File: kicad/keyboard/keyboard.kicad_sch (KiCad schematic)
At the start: 119 parts, among them SW1 MX_SWITCH, SW10 MX_SWITCH, SW11 MX_SWITCH, SW12 MX_SWITCH, SW13 MX_SWITCH, SW14 MX_SWITCH, SW15 MX_SWITCH, SW16 MX_SWITCH, SW17 MX_SWITCH, SW18 MX_SWITCH, SW19 MX_SWITCH, SW2 MX_SWITCH, SW20 MX_SWITCH, SW21 MX_SWITCH, SW22 MX_SWITCH, SW23 MX_SWITCH, SW24 MX_SWITCH, SW25 MX_SWITCH, SW26 MX_SWITCH, SW27 MX_SWITCH, SW28 MX_SWITCH, SW29 MX_SWITCH, SW3 MX_SWITCH, SW30 MX_SWITCH, SW31 MX_SWITCH, SW32 MX_SWITCH, SW33 MX_SWITCH, SW34 MX_SWITCH, SW35 MX_SWITCH, SW36 MX_SWITCH, SW37 MX_SWITCH, SW38 MX_SWITCH, SW39 MX_SWITCH, SW4 MX_SWITCH, SW40 MX_SWITCH, SW41 MX_SWITCH, SW42 MX_SWITCH, SW43 MX_SWITCH, SW44 MX_SWITCH, SW45 MX_SWITCH, SW46 MX_SWITCH, SW47 MX_SWITCH, SW48 MX_SWITCH, SW49 MX_SWITCH, SW5 MX_SWITCH, SW50 MX_SWITCH, SW51 MX_SWITCH, SW52 MX_SWITCH, SW53 MX_SWITCH, SW54 MX_SWITCH, SW55 MX_SWITCH, SW56 MX_SWITCH, SW57 MX_SWITCH, SW58 MX_SWITCH, SW59 MX_SWITCH, SW6 MX_SWITCH, SW7 MX_SWITCH, SW8 MX_SWITCH, SW9 MX_SWITCH

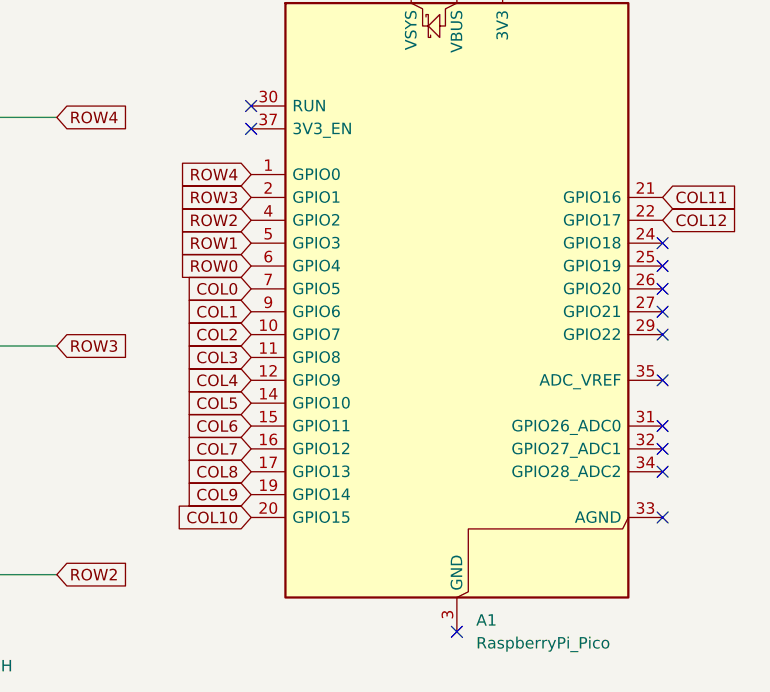
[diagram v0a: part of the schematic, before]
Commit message: Assign footprints
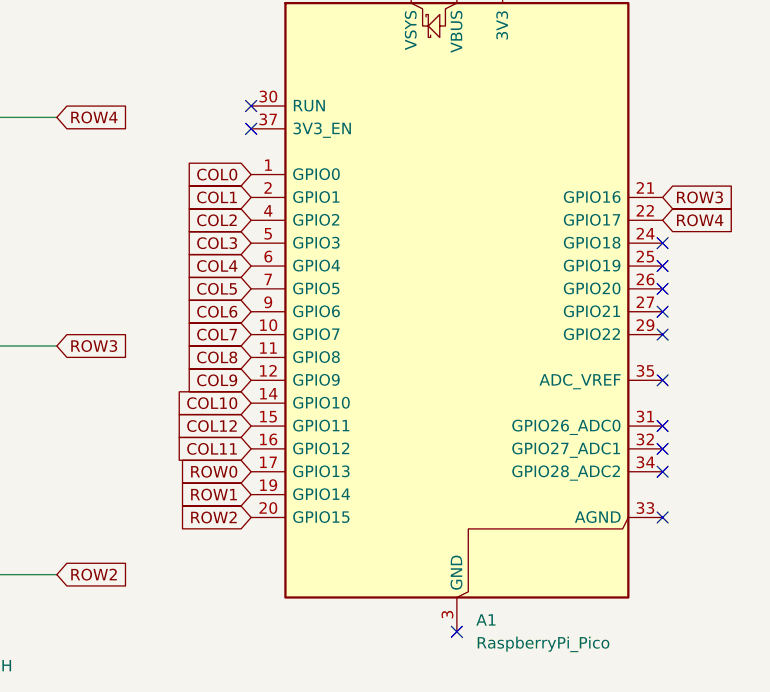
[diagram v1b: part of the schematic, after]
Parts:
- A1: footprint Module:RaspberryPi_Pico_Common_Unspecified -> Module:RaspberryPi_Pico_Common_THT
- D1, D10, D11, D12, D13, D14, D15, D16, D17, D18, D19, D2, D20, D21, D22, D23, D24, D25, D26, D27, D28, D29, D3, D30, D31, D32, D33, D34, D35, D36, D37, D38, D39, D4, D40, D41, D42, D43, D44, D45, D46, D47, D48, D49, D5, D50, D51, D52, D53, D54, D55, D56, D57, D58, D59, D6, D7, D8, D9: footprint (none) -> Diode_THT:D_DO-35_SOD27_P2.54mm_Vertical_KathodeUp
- SW1, SW10, SW11, SW12, SW13, SW14, SW15, SW16, SW17, SW18, SW19, SW2, SW20, SW21, SW22, SW23, SW24, SW25, SW26, SW27, SW28, SW29, SW3, SW30, SW31, SW32, SW33, SW34, SW35, SW36, SW37, SW38, SW39, SW4, SW40, SW41, SW42, SW43, SW44, SW45, SW46, SW47, SW48, SW49, SW5, SW50, SW51, SW52, SW53, SW54, SW55, SW56, SW57, SW58, SW59, SW6, SW7, SW8, SW9: footprint (none) -> Button_Switch_Keyboard:SW_Cherry_MX_1.00u_PCB
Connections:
- net COL0: now also A1.1 (GPIO0); no longer A1.7 (GPIO5)
- net COL1: now also A1.2 (GPIO1); no longer A1.9 (GPIO6)
- net COL10: now also A1.14 (GPIO10); no longer A1.20 (GPIO15)
- net COL11: now also A1.16 (GPIO12); no longer A1.21 (GPIO16)
- net COL12: now also A1.15 (GPIO11); no longer A1.22 (GPIO17)
- net COL2: now also A1.4 (GPIO2); no longer A1.10 (GPIO7)
- net COL3: now also A1.5 (GPIO3); no longer A1.11 (GPIO8)
- net COL4: now also A1.6 (GPIO4); no longer A1.12 (GPIO9)
- net COL5: now also A1.7 (GPIO5); no longer A1.14 (GPIO10)
- net COL6: now also A1.9 (GPIO6); no longer A1.15 (GPIO11)
- net COL7: now also A1.10 (GPIO7); no longer A1.16 (GPIO12)
- net COL8: now also A1.11 (GPIO8); no longer A1.17 (GPIO13)
- net COL9: now also A1.12 (GPIO9); no longer A1.19 (GPIO14)
- net ROW0: now also A1.17 (GPIO13); no longer A1.6 (GPIO4)
- net ROW1: now also A1.19 (GPIO14); no longer A1.5 (GPIO3)
- net ROW2: now also A1.20 (GPIO15); no longer A1.4 (GPIO2)
- net ROW3: now also A1.21 (GPIO16); no longer A1.2 (GPIO1)
- net ROW4: now also A1.22 (GPIO17); no longer A1.1 (GPIO0)
